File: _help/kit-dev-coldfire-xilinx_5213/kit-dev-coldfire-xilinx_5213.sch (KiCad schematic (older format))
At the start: 68 parts, among them Q1 3906, U1 MCF5213-LQFP100, U2 74AHC1G14, Y1 8MHz

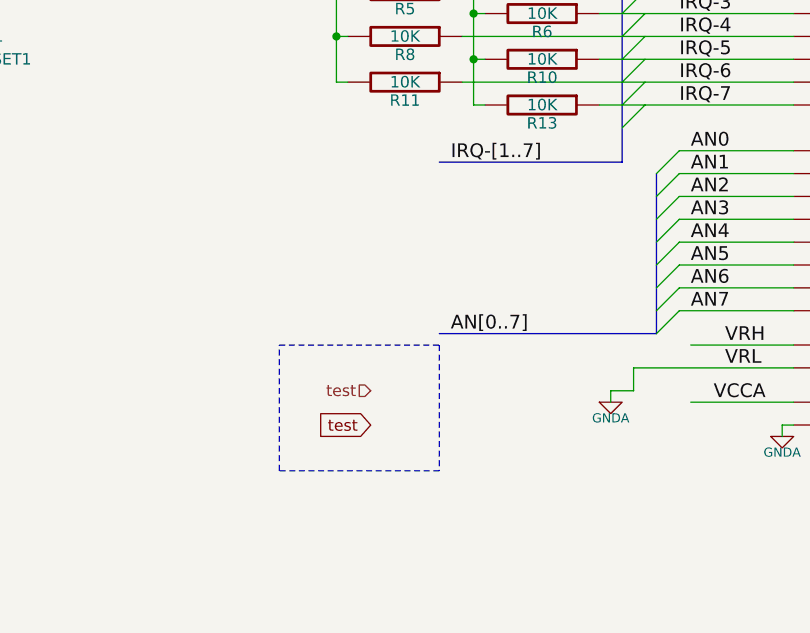
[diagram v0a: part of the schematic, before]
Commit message: Updated example
- prepared pcb side for screenshots
- added ERC error source and subsheet to schematic screenshot area.
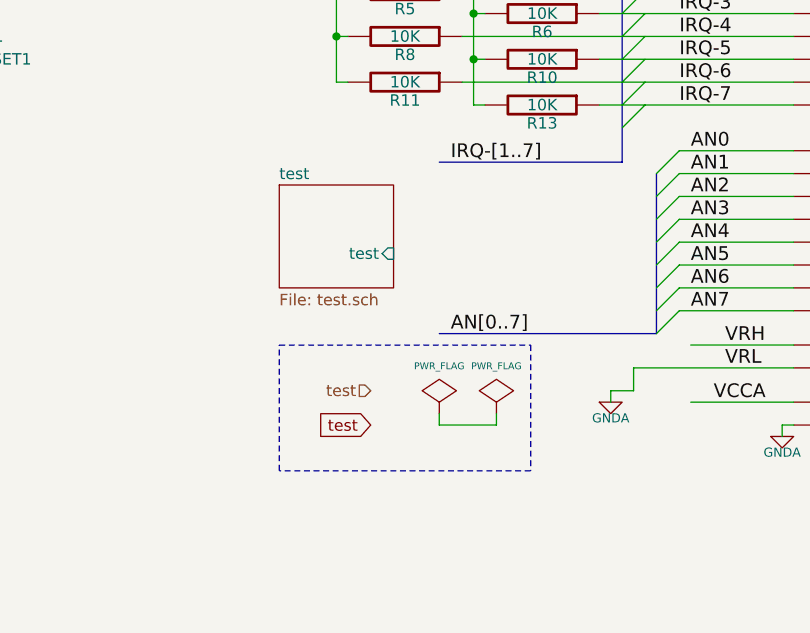
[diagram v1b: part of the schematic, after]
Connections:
- wire segments 367 -> 370
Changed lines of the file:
@@
 EESchema Schematic File Version 4
 LIBS:kit-dev-coldfire-xilinx_5213-cache
-EELAYER 26 0
+EELAYER 29 0
 EELAYER END
 $Descr A3 16535 11693
 encoding utf-8
-Sheet 1 3
+Sheet 1 4
 Title "Dev kit coldfire 5213"
 Date "Sun 22 Mar 2015"
@@
 test
 Wire Notes Line
-	3900 6700 4600 6700
+	3900 6700 5000 6700
 Wire Notes Line
-	4600 6700 4600 7250
+	5000 6700 5000 7250
 Wire Notes Line
-	4600 7250 3900 7250
+	5000 7250 3900 7250
 Wire Notes Line
 	3900 7250 3900 6700
 Wire Wire Line
 	5300 5050 6150 5050
+$Comp
+L kit-dev-coldfire-xilinx_5213_schlib:PWR_FLAG #FLG0101
+U 1 1 5CCC9B96
+P 4600 7000
+F 0 "#FLG0101" H 4600 7095 30  0001 C CNN
+F 1 "PWR_FLAG" H 4600 7208 30  0000 C CNN
+F 2 "" H 4600 7000 60  0000 C CNN
+F 3 "" H 4600 7000 60  0000 C CNN
+	1    4600 7000
+	1    0    0    -1
+$EndComp
+$Comp
+L kit-dev-coldfire-xilinx_5213_schlib:PWR_FLAG #FLG0102
+U 1 1 5CD50A93
+P 4850 7000
+F 0 "#FLG0102" H 4850 7095 30  0001 C CNN
+F 1 "PWR_FLAG" H 4850 7208 30  0000 C CNN
+F 2 "" H 4850 7000 60  0000 C CNN
+F 3 "" H 4850 7000 60  0000 C CNN
+	1    4850 7000
+	1    0    0    -1
+$EndComp
+Wire Wire Line
+	4850 7000 4850 7050
+Wire Wire Line
+	4850 7050 4600 7050
+Wire Wire Line
+	4600 7050 4600 7000
+$Sheet
+S 3900 6000 500  450
+U 5CD8040D
+F0 "test" 50
+F1 "test.sch" 50
+F2 "test" I R 4400 6300 50
+$EndSheet
 Wire Wire Line
 	5300 5650 6150 5650
